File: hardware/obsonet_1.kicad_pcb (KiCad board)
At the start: 2 copper layers, 100 x 64.8 mm, 35 parts, among them CON1 CART_BOARD, CON2 RJ45_H, IC1 M29F400M, IC2 93C46_SOIC, IC3 74HC133, IC4 RTL8019AS, IC5 93C46_DIL, IC6 GAL16V8D, Q1 20MHz, SW1 SWITCH

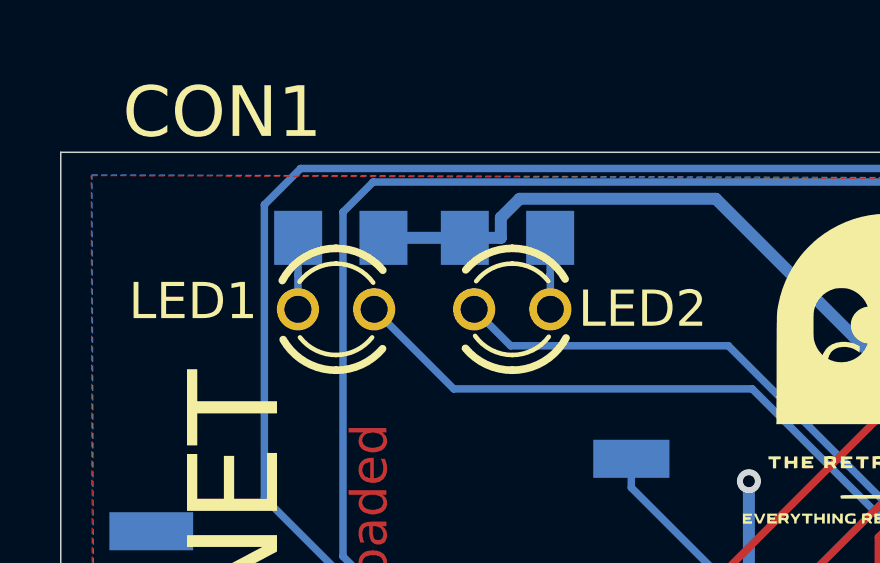
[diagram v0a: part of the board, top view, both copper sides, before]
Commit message: Updated licensing and README
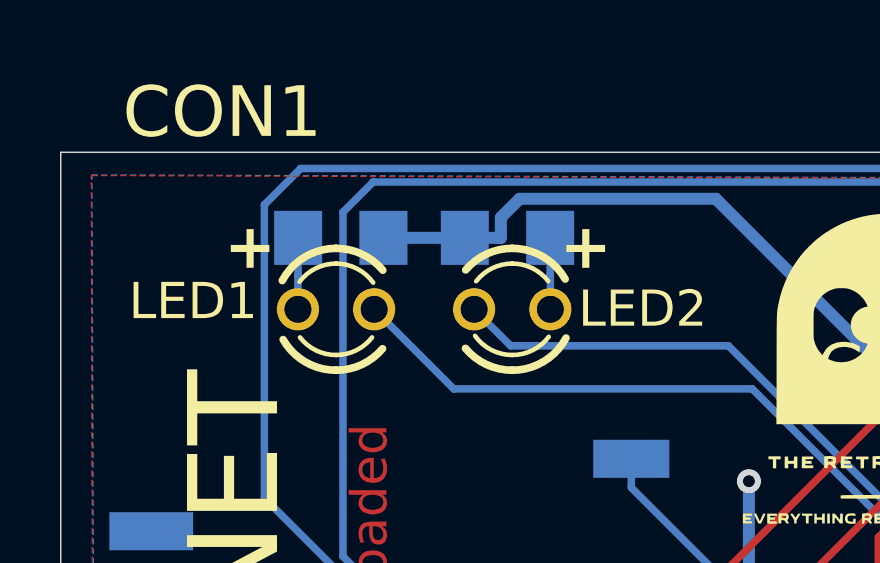
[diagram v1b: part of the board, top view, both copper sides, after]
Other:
- board text added: "+"
